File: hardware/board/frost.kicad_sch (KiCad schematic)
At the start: 1 part, among them U1 RK3568

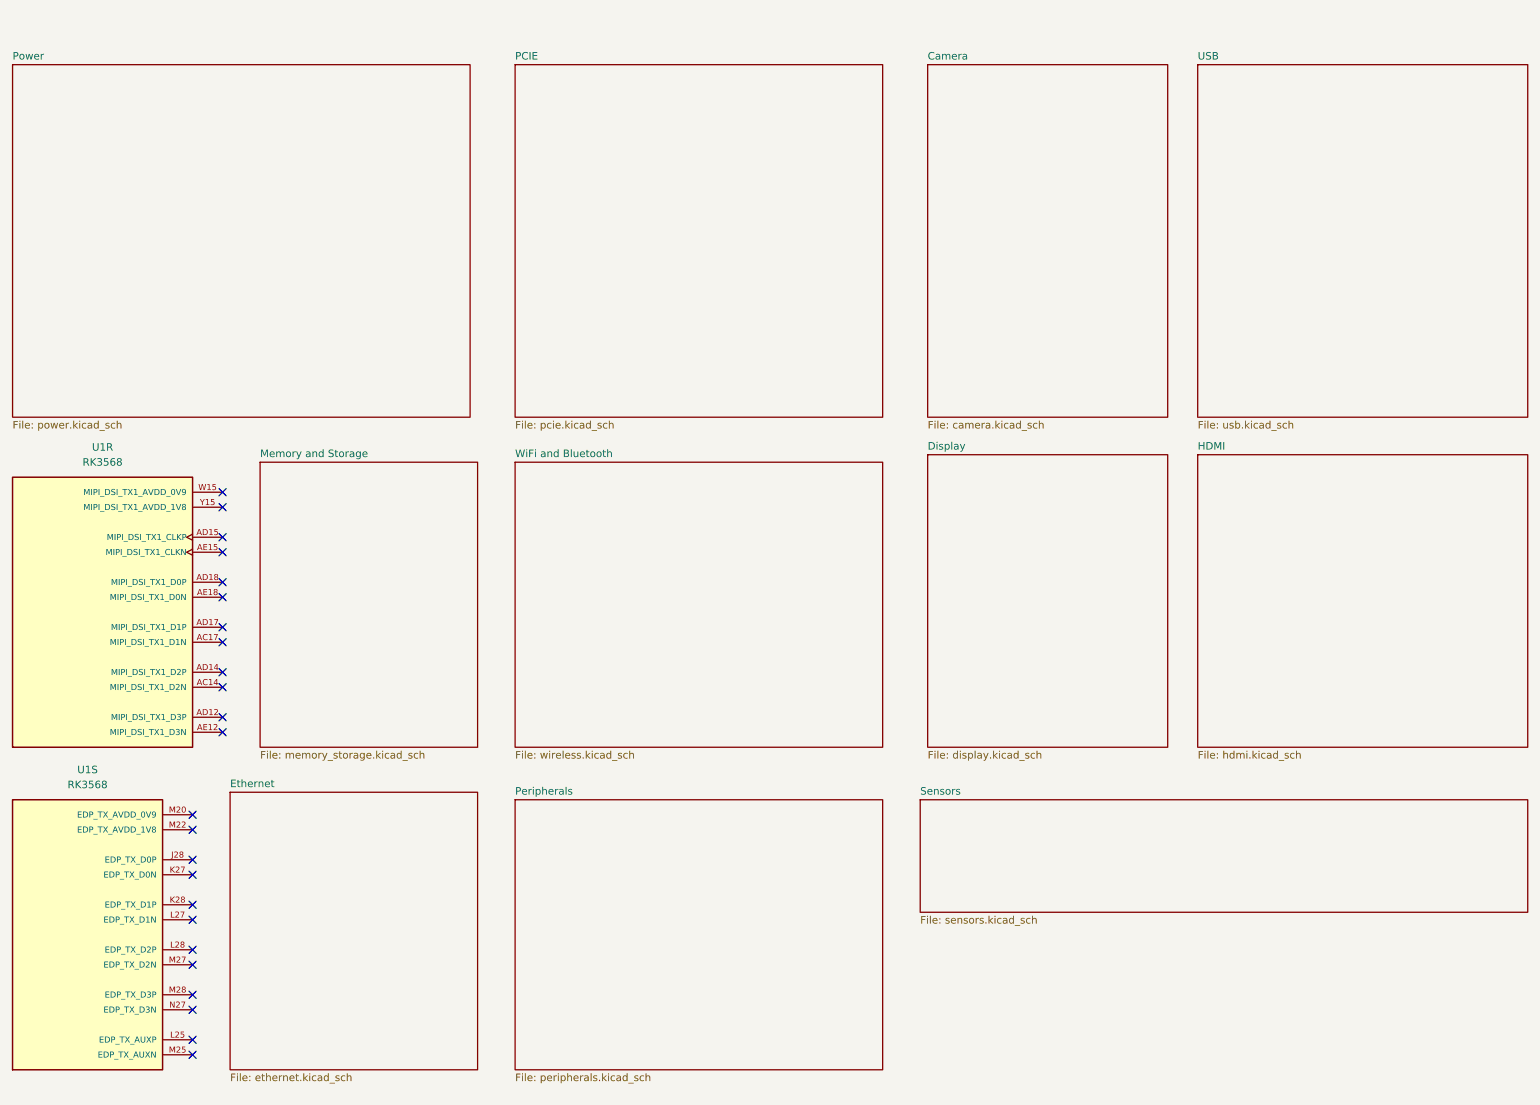
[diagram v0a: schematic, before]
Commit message: finished beautifying schematic
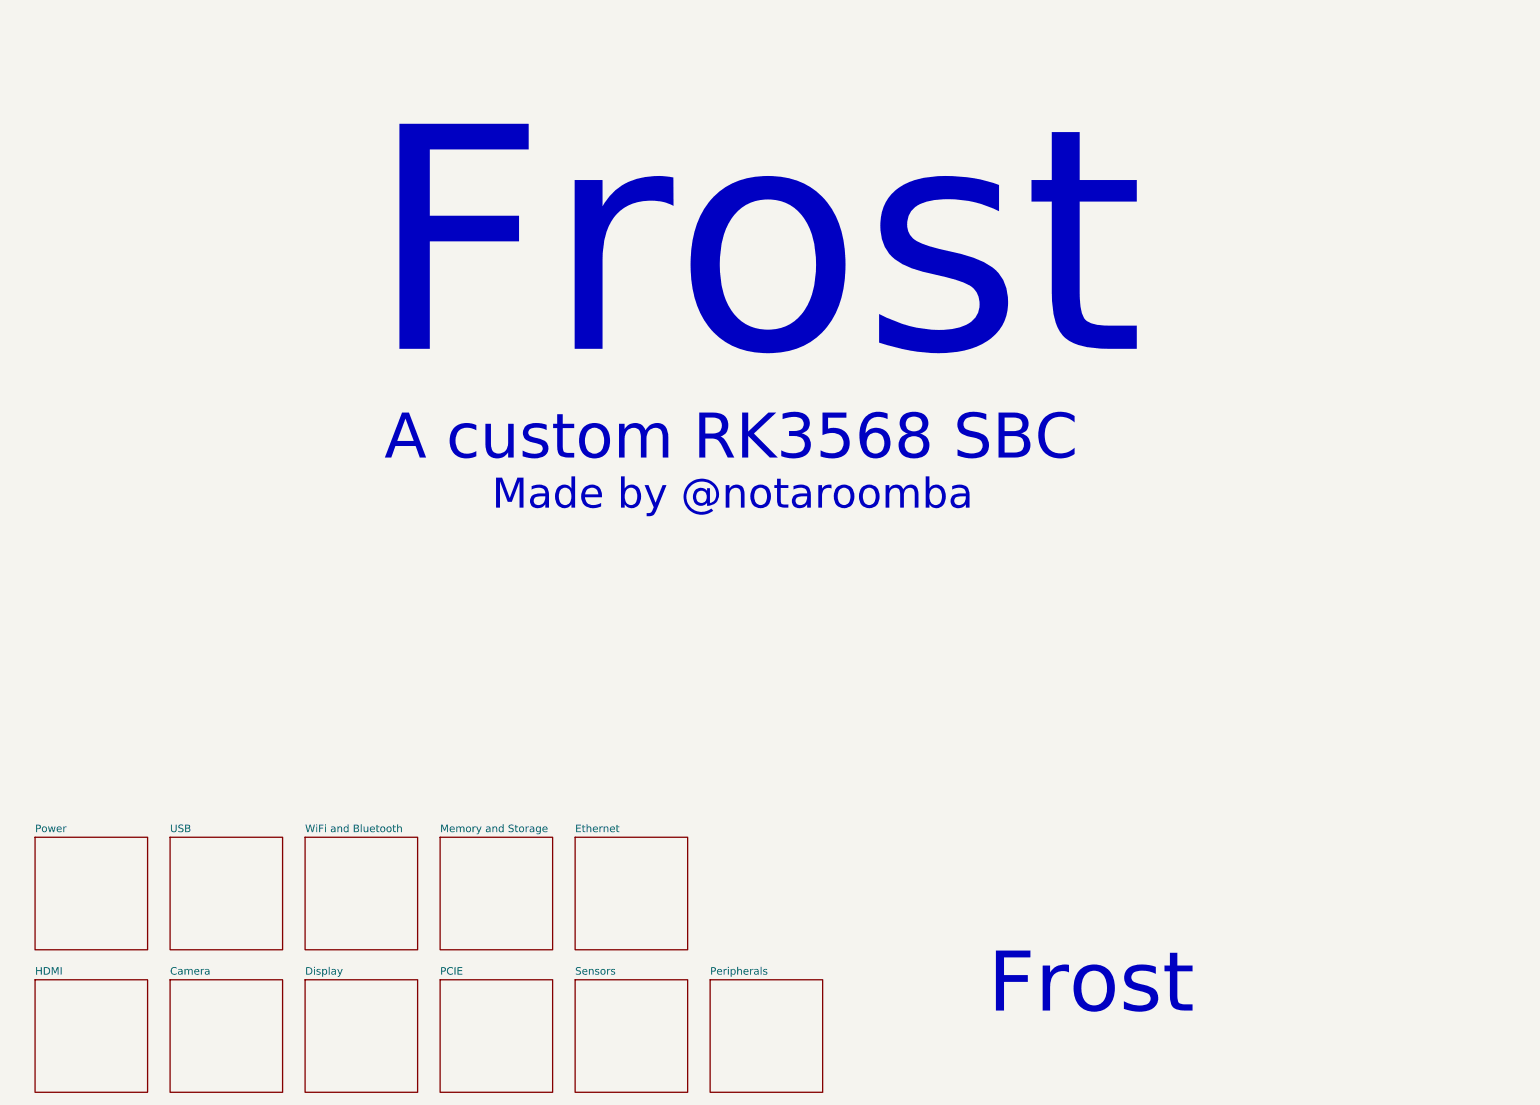
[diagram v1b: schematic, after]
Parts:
- removed U1: RK3568, RK3568:BGA636C65P28X28_1900X1900X168, symbol RK3568:RK3568
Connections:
- no-connect marks 24 -> 0
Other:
- note added: "A custom RK3568 SBC"
- note added: "Frost"
- note added: "Made by @notaroomba"
